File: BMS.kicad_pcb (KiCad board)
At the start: 2 copper layers, 62 parts, among them J1 Screw_Terminal_01x02, J5 BATT_PACK -, J6 PACK _PACK -, Q22 CSD19531Q5A, Q23 CSD19531Q5A, Q24 CSD19531Q5A, T3 EE20_10_6_750811647, U1 TL431DBZ, U18 VIPer26LD, U2 PC817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

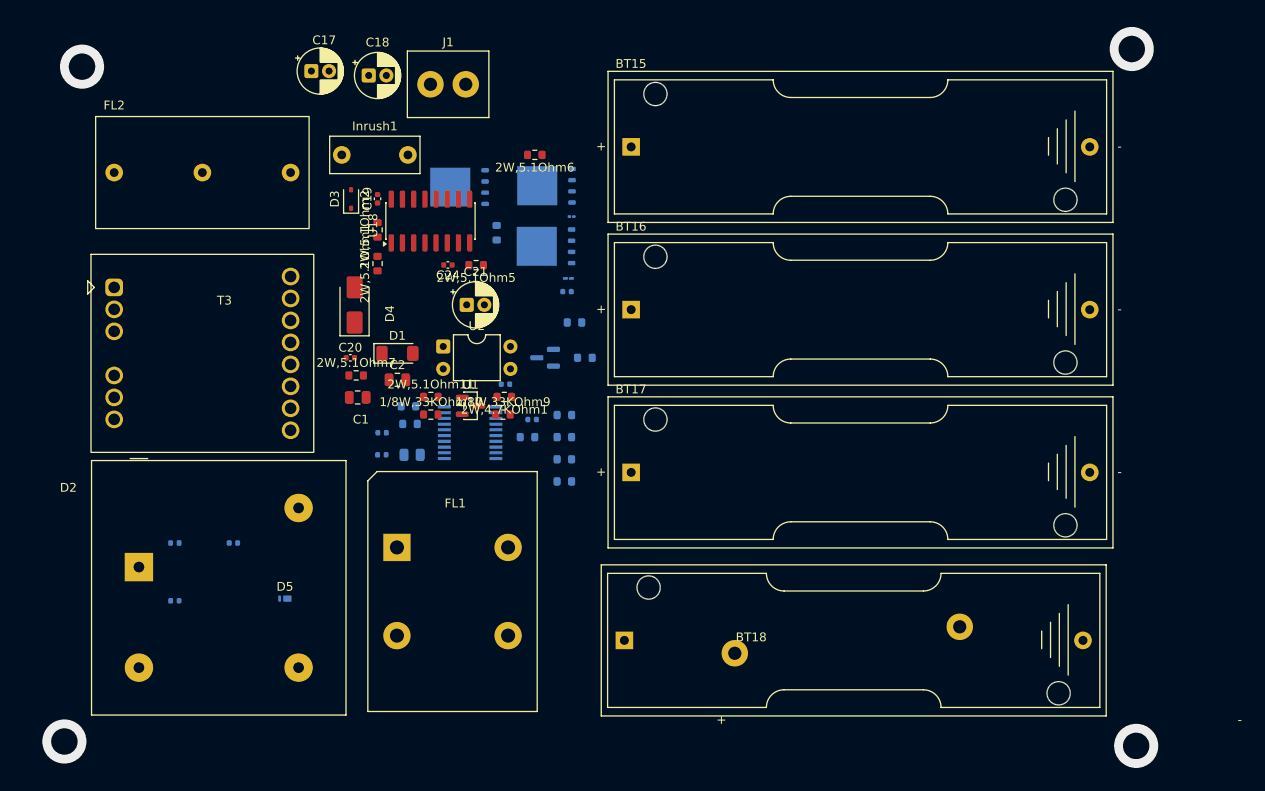
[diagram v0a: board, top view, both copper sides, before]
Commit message: Update PCB stackup, footprints, and add backups
Add multiple BMS backup archives and project PNG; modify BMS.kicad_pcb with an explicit stackup (layers, thicknesses, dielectric), enable zone_defaults, and update many footprints and component definitions. Changes include footprint replacements and edits (resistor/pad sizes, SMD 0402→0805 adjustments, pad positions/nets, UUIDs), added/adjusted 3D model references and part rotations/offsets, and new LED/resistor SMD footprints. Also update related KiCad project files and lock files.
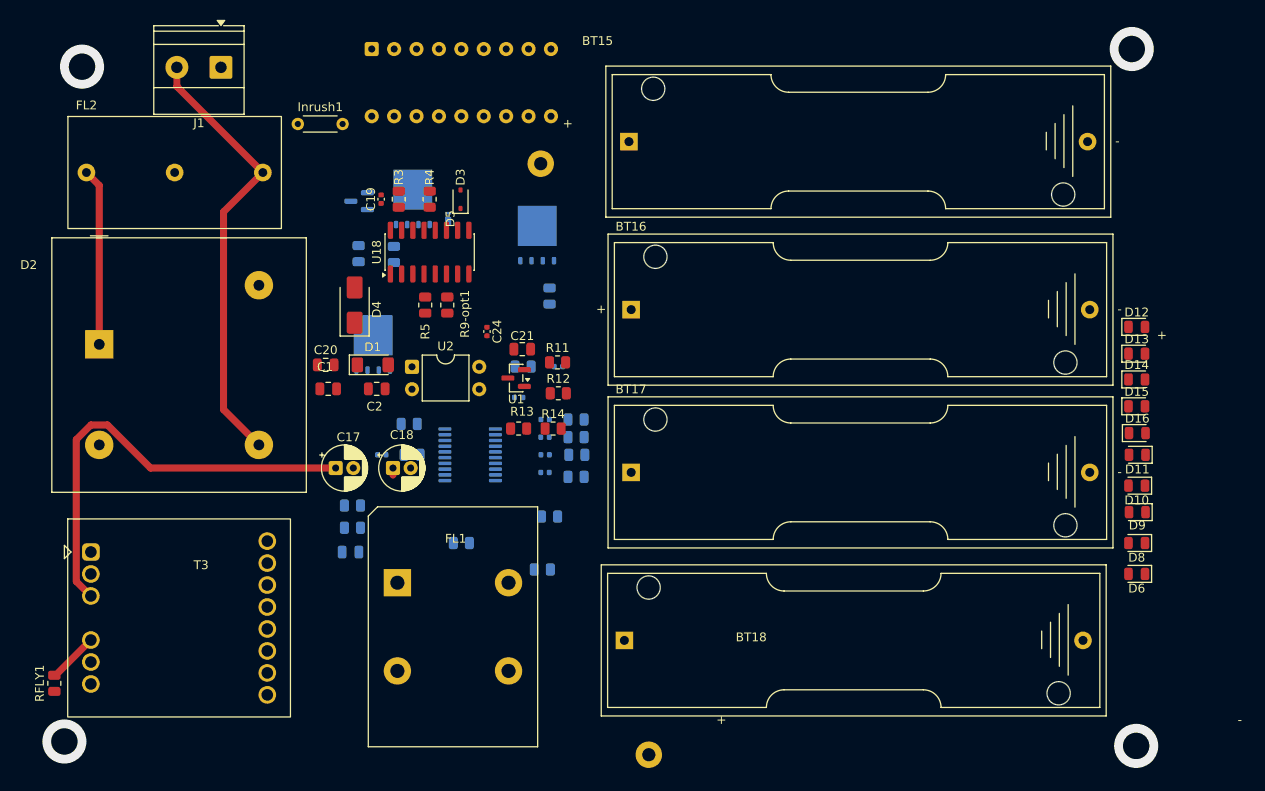
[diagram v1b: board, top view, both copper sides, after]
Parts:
- removed 1/8W,33KOhm10, 1/8W,33KOhm9, 2W,4.7KOhm1, 2W,5.1Ohm1, 2W,5.1Ohm11, 2W,5.1Ohm13, 2W,5.1Ohm17, 2W,5.1Ohm18, 2W,5.1Ohm19, 2W,5.1Ohm2, 2W,5.1Ohm20, 2W,5.1Ohm21, 2W,5.1Ohm22, 2W,5.1Ohm5, 2W,5.1Ohm6, 2W,5.1Ohm7: R, Resistor_SMD:R_0603_1608Metric
- added 10k2: 10k, Resistor_SMD:R_0805_2012Metric, B.Cu at (132.7, 95.3)
- added 10k3: 10k, Resistor_SMD:R_0805_2012Metric, B.Cu at (132.7, 97.8)
- added C3: 470uF, Capacitor_SMD:C_0805_2012Metric, B.Cu at (132.4, 100.5)
- added D10: LED, LED_SMD:LED_0805_2012Metric, F.Cu at (221.6, 93.0)
- added D11: LED, LED_SMD:LED_0805_2012Metric, F.Cu at (221.6, 89.5)
- added D12: LED, LED_SMD:LED_0805_2012Metric, F.Cu at (221.6, 75.0)
- added D13: LED, LED_SMD:LED_0805_2012Metric, F.Cu at (221.6, 78.0)
- added D14: LED, LED_SMD:LED_0805_2012Metric, F.Cu at (221.6, 81.0)
- added D15: LED, LED_SMD:LED_0805_2012Metric, F.Cu at (221.6, 84.0)
- added D16: LED, LED_SMD:LED_0805_2012Metric, F.Cu at (221.6, 87.0)
- added D6: LED, LED_SMD:LED_0805_2012Metric, F.Cu at (221.6, 103.0)
- added D8: LED, LED_SMD:LED_0805_2012Metric, F.Cu at (221.6, 99.5)
- added D9: LED, LED_SMD:LED_0805_2012Metric, F.Cu at (221.6, 96.0)
- added R11: R, Resistor_SMD:R_0805_2012Metric, F.Cu at (155.9, 79.0)
- added R12: R, Resistor_SMD:R_0805_2012Metric, F.Cu at (156.0, 82.5)
- added R13: R, Resistor_SMD:R_0805_2012Metric, F.Cu at (151.5, 86.5)
- added R14: R, Resistor_SMD:R_0805_2012Metric, F.Cu at (155.4, 86.5)
- added R3: 51k, Resistor_SMD:R_0805_2012Metric, F.Cu at (137.9, 60.5)
- added R4: 51k, Resistor_SMD:R_0805_2012Metric, F.Cu at (141.4, 60.5)
- added R5: 10k, Resistor_SMD:R_0805_2012Metric, F.Cu at (140.9, 72.5)
- added R9-opt1: 100, Resistor_SMD:R_0805_2012Metric, F.Cu at (143.4, 72.5)
- added RFLY1: 100, Resistor_SMD:R_0805_2012Metric, F.Cu at (98.9, 115.4)
- added RVO1: R, Resistor_SMD:R_0805_2012Metric, B.Cu at (152.0, 79.5)
- added Rbat1: 1k, Resistor_SMD:R_0805_2012Metric, B.Cu at (158.0, 85.5)
- added Rbat2: 1k, Resistor_SMD:R_0805_2012Metric, B.Cu at (158.0, 87.5)
- added Rbat3: 1k, Resistor_SMD:R_0805_2012Metric, B.Cu at (158.1, 89.5)
- added Rbat4: 1k, Resistor_SMD:R_0805_2012Metric, B.Cu at (158.0, 92.0)
- added Rsrn1: 100, Resistor_SMD:R_0805_2012Metric, B.Cu at (155.0, 96.5)
- added Rsrp1: 100, Resistor_SMD:R_0805_2012Metric, B.Cu at (154.2, 102.5)
- added U3: LM3914N, Package_DIP:DIP-18_W7.62mm, B.Cu at (134.8, 43.5)
- 1M3, 1M5, 6ohm1: footprint Resistor_SMD:R_0603_1608Metric -> Resistor_SMD:R_0805_2012Metric
- C20: footprint Capacitor_SMD:C_0402_1005Metric -> Capacitor_SMD:C_0805_2012Metric
- C21: footprint Capacitor_THT:CP_Radial_D5.0mm_P2.00mm -> Capacitor_SMD:C_0805_2012Metric
- Inrush1: footprint Capacitor_THT:C_Rect_L10.0mm_W4.0mm_P7.50mm_MKS4 -> Resistor_THT:R_Axial_DIN0204_L3.6mm_D1.6mm_P5.08mm_Horizontal
- J1: footprint TerminalBlock_MetzConnect:TerminalBlock_MetzConnect_360291_1x01_Horizontal_ScrewM3.0_Boxed -> TerminalBlock_Phoenix:TerminalBlock_Phoenix_MKDS-1,5-2_1x02_P5.00mm_Horizontal
- R1: footprint Resistor_SMD:R_01005_0402Metric_Pad0.57x0.30mm_HandSolder -> Resistor_SMD:R_0805_2012Metric
- R2: footprint Resistor_SMD:R_01005_0402Metric -> Resistor_SMD:R_0805_2012Metric
- U21: footprint bms qb:PW20_TEX -> Package_SO:TSSOP-20_4.4x6.5mm_P0.65mm
- moved J5 59.7 mm to (154.0, 56.5)
- moved D5 46.9 mm to (143.5, 62.7), turned to 90 degrees
- moved C34 45.1 mm to (154.5, 89.5)
- moved C17 45.1 mm to (130.8, 91.0)
- moved C18 44.6 mm to (137.2, 91.0)
- moved C33 43.6 mm to (154.5, 87.5)
- moved J6 38.1 mm to (166.2, 123.5)
- moved C38 38.0 mm to (154.5, 85.5)
- moved T3 30.1 mm to (103.0, 100.5)
- moved D7 27.6 mm to (133.4, 60.8)
- moved D2 25.6 mm to (104.0, 77.0)
- moved J1 23.8 mm to (117.8, 45.6), turned to 180 degrees
- moved R2 20.6 mm to (137.3, 66.8), turned to 90 degrees
- moved Q23 20.4 mm to (135.0, 77.0), turned to 90 degrees
- moved 1M3 15.8 mm to (133.3, 66.7)
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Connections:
- BT18 pad 1: Net-(BT18-+) -> V+
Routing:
- net Net-(C17-Pad1): track 0.00 -> 52.2 mm
- net Net-(D2--): track 0.00 -> 50.3 mm
- net Net-(D2-+): track 0.00 -> 20.1 mm
- net Net-(RFLY1-Pad2): track 0.00 -> 5.80 mm

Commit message: routing
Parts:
- C19, C24: footprint Capacitor_SMD:C_0402_1005Metric -> Capacitor_THT:CP_Radial_D5.0mm_P2.00mm
- moved T3 32.2 mm to (135.1, 99.5)
- moved RFLY1 32.2 mm to (131.0, 114.4)
- moved R3 32.1 mm to (144.5, 91.9)
- moved R4 32.1 mm to (147.5, 92.0), turned to -90 degrees
- moved C19 32.0 mm to (138.0, 92.5)
- moved D3 26.4 mm to (138.0, 86.0), turned to 0 degrees
- moved D4 23.1 mm to (155.5, 77.5), turned to 180 degrees
- moved R13 21.6 mm to (153.0, 65.0)
- moved U1 21.6 mm to (145.5, 60.0)
- moved FL1 21.3 mm to (117.0, 99.2), turned to -90 degrees
- moved U18 20.7 mm to (148.5, 86.0)
- moved FL2 19.0 mm to (121.5, 58.0), turned to 180 degrees
- moved R14 18.7 mm to (157.9, 68.0), turned to 180 degrees
- moved D2 17.9 mm to (121.0, 82.3), turned to 180 degrees
- moved C21 17.1 mm to (153.0, 60.5)
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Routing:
- net SRP: track 0.00 -> 114.3 mm, vias 0 -> 1
- net Net-(D4-A): track 0.00 -> 57.2 mm
- net 5: track 0.00 -> 36.0 mm
- net Net-(D2-Pad4): track 0.00 -> 35.2 mm
- net Net-(U1-REF): track 0.00 -> 24.1 mm
- net Net-(D2-+): track 20.1 -> 40.9 mm
- net Net-(C17-Pad1): track 52.2 -> 36.1 mm
- net Net-(D2-Pad2): track 0.00 -> 14.7 mm
- net Net-(J1-Pin_1): track 0.00 -> 14.7 mm
- net Net-(D2--): track 50.3 -> 36.0 mm
- net Net-(D3-K): track 0.00 -> 9.88 mm
- net Net-(C20-Pad2): track 0.00 -> 8.20 mm
- net Net-(U1-K): track 0.00 -> 7.33 mm
- net Net-(D3-A): track 0.00 -> 6.03 mm
- net FB: track 0.00 -> 5.97 mm
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
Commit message: Update of routing
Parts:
- added TH2: Thermistor, Resistor_SMD:R_0805_2012Metric, B.Cu at (139.5, 90.0)
- moved C3 49.0 mm to (131.4, 51.5)
- moved D10 25.1 mm to (223.5, 68.0)
- moved D6 25.1 mm to (223.5, 78.0)
- moved D8 25.1 mm to (223.5, 74.5)
- moved D9 24.6 mm to (223.6, 71.5)
- moved Rsrp1 22.5 mm to (139.5, 85.5)
- moved C36 14.1 mm to (148.5, 96.0)
- moved C37 13.7 mm to (140.5, 101.0)
- moved D12 10.2 mm to (223.5, 85.0)
- moved D14 10.2 mm to (223.5, 91.0)
- moved D15 10.2 mm to (223.5, 94.0)
- moved D13 10.2 mm to (223.5, 88.1)
- moved D16 10.2 mm to (223.6, 97.1)
- moved Inrush1 8.62 mm to (123.0, 44.1), turned to -90 degrees
- moved D11 8.23 mm to (223.6, 81.5)
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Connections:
- net Net-(D5-A) renamed V-
- 6ohm1 pad 1: SRP -> VO
- BT17 pad 2: SRP -> VO
- C1 pad 1: SRP -> VO
- C1 pad 2: SRP -> VO
- C17 pad 2: SRP -> VO
- C18 pad 2: SRP -> VO
- C2 pad 1: SRP -> VO
- C2 pad 2: SRP -> VO
- C20 pad 1: Net-(D4-A) -> Net-(C20-Pad1)
- C20 pad 2: Net-(C20-Pad2) -> Net-(D4-A)
- C24 pad 2: SRP -> VO
- C30 pad 1: SRP -> VO
- C31 pad 1: SRP -> VO
- C33 pad 1: SRP -> VO
- C34 pad 1: SRP -> VO
- C35 pad 1: SRP -> VO
- C36 pad 1: SRN -> SRP
- C36 pad 2: SRP -> SRN
- C37 pad 1: SRP -> VO
- C38 pad 1: SRP -> VO
- D1 pad 1: SRP -> VO
- D1 pad 2: SRP -> VO
- D15 pad 1: Net-(D14-K) -> unconnected-(D15-K-Pad1)
- D16 pad 1: Net-(D14-K) -> Net-(D16-K)
- D4 pad 1: SRP -> VO
- FL1 pad 3: SRP -> VO
- FL2 pad 3: SRP -> VO
- Q22 pad 1: SRP -> VO
- Q22 pad 2: SRP -> VO
- Q22 pad 3: SRP -> VO
- Q23 pad 4: SRP -> VO
- R11 pad 2: SRP -> VO
- R14 pad 1: SRP -> VO
- R5 pad 2: SRP -> VO
- R9-opt1 pad 1: Net-(C20-Pad2) -> Net-(C20-Pad1)
- R9-opt1 pad 2: SRP -> VO
- RFLY1 pad 1: SRP -> VO
- RVO1 pad 2: SRP -> VO
- Rsrp1 pad 2: SRP -> VO
- T3 pad 10: SRP -> VO
- T3 pad 13: SRP -> VO
- U1 pad 3: SRP -> VO
- U18 pad 1: SRP -> VO
- U18 pad 2: SRP -> VO
- U21 pad 17: SRP -> VO
- U21 pad 18: SRP -> VO
- U21 pad 19: SRP -> VO
- U21 pad 20: SRP -> VO
- U21 pad 8: SRP -> VO
- U3 pad 10: Net-(D14-K) -> Net-(D16-K)
- U3 pad 11: Net-(D14-K) -> unconnected-(U3-LED9-Pad11)
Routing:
- net SRP: track 114.3 -> 0.00 mm, vias 1 -> 0
- net VO: track 0.00 -> 109.1 mm
- net Net-(R12-Pad2): track 0.00 -> 13.1 mm
- net Net-(D4-A): track 57.2 -> 68.4 mm
- net Net-(C20-Pad2): track 8.20 -> 0.00 mm
- net Net-(U21-TS): track 0.00 -> 6.43 mm
- net FB: track 5.97 -> 11.1 mm
- net 5: track 36.0 -> 31.3 mm
- net Net-(J1-Pin_1): track 14.7 -> 10.1 mm
- net Net-(U21-VTB): track 0.00 -> 4.12 mm
- net LD: track 0.00 -> 3.65 mm
- net Net-(D2-+): track 40.9 -> 37.6 mm
- net Net-(U21-VDD): track 0.00 -> 3.26 mm
- net Net-(C30-Pad2): track 0.00 -> 2.97 mm
- net Net-(U1-REF): track 24.1 -> 21.2 mm
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
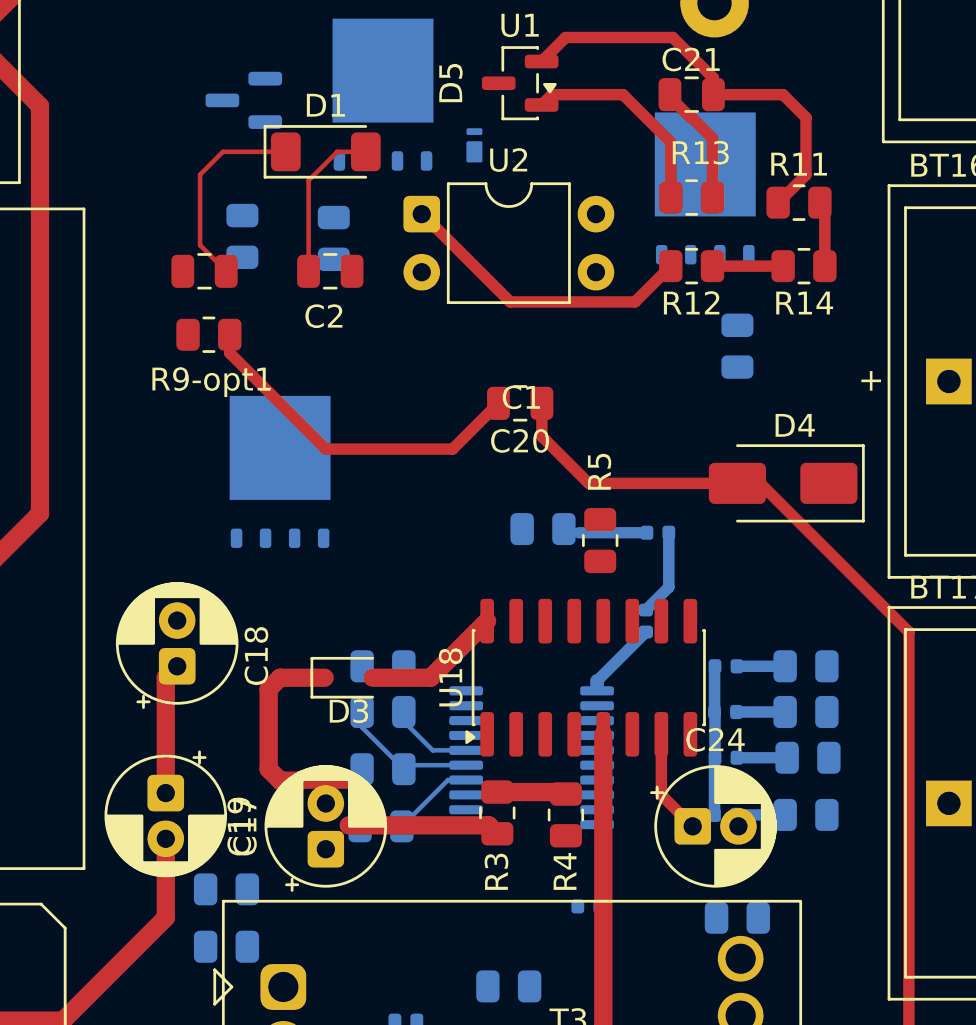
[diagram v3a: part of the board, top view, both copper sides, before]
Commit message: Updated GND via and holes
GND was missdirected at VO point and had to be fixed
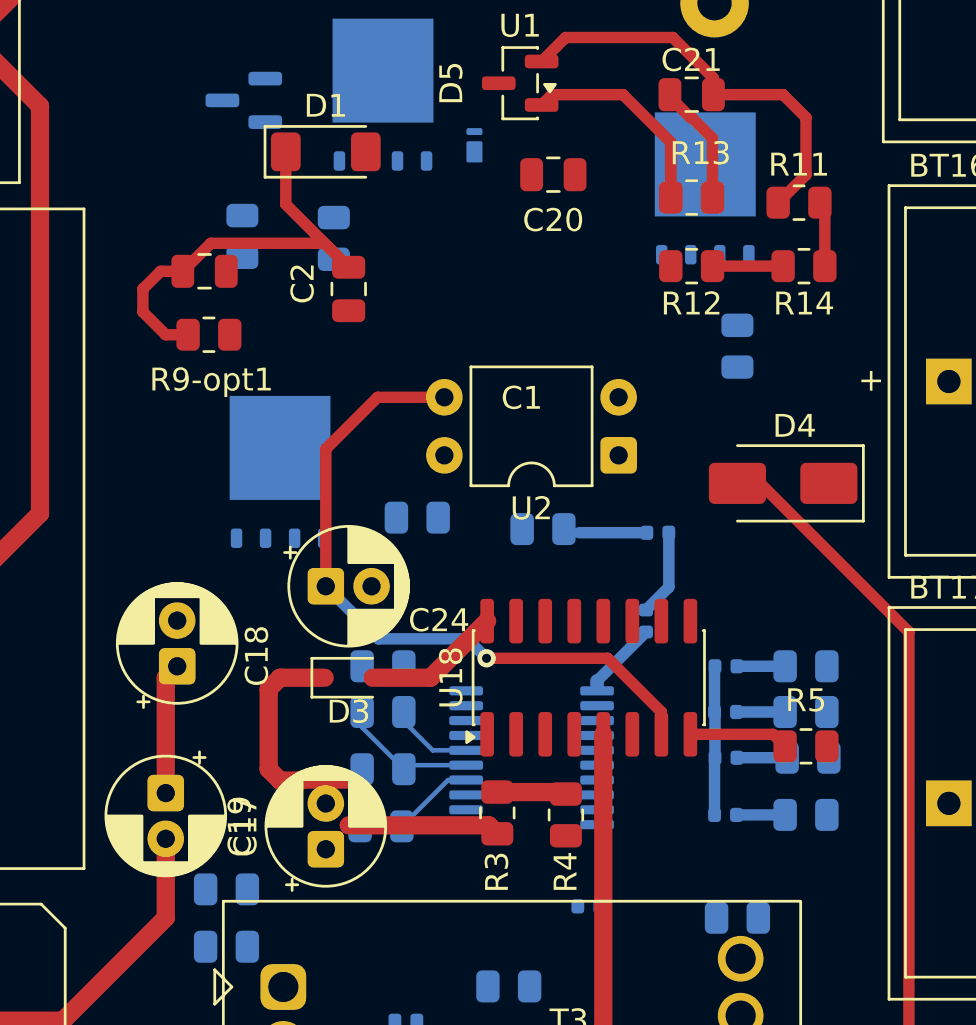
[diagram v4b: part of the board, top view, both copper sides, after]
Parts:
- added R6: 100 Ohm, Resistor_SMD:R_0805_2012Metric, B.Cu at (141.0, 79.0)
- moved C24 19.2 mm to (137.0, 82.0)
- moved U2 13.6 mm to (149.8, 76.3), turned to 180 degrees
- moved R5 12.7 mm to (158.0, 89.0), turned to 0 degrees
- moved C20 10.1 mm to (146.9, 64.0)
- moved C2 1.12 mm to (138.0, 69.0), turned to -90 degrees
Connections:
- net 5 renamed VDD_U18
- 6ohm1 pad 1: VO -> GND
- BT17 pad 2: VO -> GND
- C1 pad 2: VO -> GND
- C17 pad 2: VO -> GND
- C18 pad 2: VO -> GND
- C2 pad 2: VO -> GND
- C20 pad 1: Net-(C20-Pad1) -> (no net)
- C20 pad 2: Net-(D4-A) -> (no net)
- C24 pad 2: VO -> GND
- C30 pad 1: VO -> GND
- C33 pad 1: VO -> GND
- C34 pad 1: VO -> GND
- C35 pad 1: VO -> GND
- C37 pad 1: VO -> GND
- C38 pad 1: VO -> GND
- D1 pad 2: VO -> GND
- D15 pad 1: unconnected-(D15-K-Pad1) -> Net-(D15-K)
- FL1 pad 3: VO -> GND
- FL2 pad 3: VO -> GND
- Q22 pad 1: VO -> GND
- Q22 pad 2: VO -> GND
- Q22 pad 3: VO -> GND
- Q23 pad 4: VO -> Net-(Q23-G)
- R14 pad 1: VO -> GND
- R5 pad 2: VO -> GND
- RFLY1 pad 1: VO -> GND
- Rsrp1 pad 2: VO -> GND
- T3 pad 10: VO -> GND
- T3 pad 13: VO -> GND
- TH2 pad 2: VO -> GND
- U1 pad 3: VO -> GND
- U18 pad 1: VO -> GND
- U18 pad 2: VO -> GND
- U21 pad 17: VO -> GND
- U21 pad 18: VO -> GND
- U21 pad 19: VO -> GND
- U21 pad 20: VO -> GND
- U21 pad 8: VO -> GND
- U3 pad 11: unconnected-(U3-LED9-Pad11) -> Net-(D15-K)
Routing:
- net GND: track 0.00 -> 93.1 mm
- net VO: track 109.1 -> 26.5 mm
- net Net-(D4-A): track 68.4 -> 42.5 mm
- net FB: track 11.1 -> 30.1 mm, vias 0 -> 1
- net Net-(R12-Pad2): track 13.1 -> 0.00 mm
- net Net-(U18-COMP): track 0.00 -> 4.36 mm

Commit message: Routing update
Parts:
- moved D7 56.4 mm to (106.0, 110.0)
- moved Q24 54.6 mm to (111.7, 107.5), turned to 180 degrees
- moved D5 54.2 mm to (117.0, 110.0), turned to -90 degrees
- moved 1M3 47.5 mm to (106.0, 105.5), turned to 180 degrees
- moved R2 44.2 mm to (117.0, 106.0)
- moved R6 38.2 mm to (105.5, 65.0), turned to -90 degrees
- moved Q23 26.5 mm to (111.0, 65.8), turned to 0 degrees
- moved C20 25.4 mm to (153.5, 88.5), turned to -90 degrees
- moved J5 18.4 mm to (166.5, 43.0)
- moved C19 8.51 mm to (136.5, 85.0), turned to -90 degrees
- moved C21 8.50 mm to (157.0, 68.0)
- moved 6ohm1 8.05 mm to (144.1, 91.5)
- moved C37 8.05 mm to (139.6, 93.0)
- moved R5 7.01 mm to (151.0, 88.6), turned to -90 degrees
- moved C17 6.52 mm to (129.5, 84.5)
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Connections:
- 1M5 pad 2: V- -> PACK-
- 6ohm1 pad 2: Net-(J5-Pin_1) -> PACK-
- C20 pad 1: (no net) -> Net-(C20-Pad1)
- C20 pad 2: (no net) -> Net-(D4-A)
- D5 pad 2: V- -> PACK-
- J5 pad 1: Net-(J5-Pin_1) -> PACK-
- Q24 pad 5: V- -> PACK-
- Rsrn1 pad 2: Net-(J5-Pin_1) -> PACK-
- U2 pad 1: Net-(R12-Pad2) -> VDD_U18
- U2 pad 2: Net-(U1-K) -> FB
- U2 pad 3: FB -> Net-(U1-K)
- U2 pad 4: VDD_U18 -> Net-(R12-Pad2)
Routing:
- net GND: track 93.1 -> 6.52 mm, vias 0 -> 4
- net VO: track 26.5 -> 82.3 mm
- net CHG: track 0.00 -> 48.0 mm
- net Net-(D7-A): track 0.00 -> 44.2 mm
- net Net-(C17-Pad1): track 38.4 -> 58.4 mm
- net Net-(R12-Pad2): track 0.00 -> 15.6 mm
- net Net-(D4-A): track 42.5 -> 28.0 mm
- net FB: track 30.1 -> 16.6 mm
- net Net-(D3-A): track 6.03 -> 15.4 mm
- net Net-(U1-K): track 9.11 -> 18.4 mm
- net Net-(U1-REF): track 21.2 -> 12.3 mm
- net Net-(D5-K): track 0.00 -> 7.31 mm
- net Net-(Q24-G): track 0.00 -> 5.58 mm
- net Net-(D3-K): track 9.88 -> 5.69 mm
- net VDD_U18: track 31.3 -> 34.8 mm
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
